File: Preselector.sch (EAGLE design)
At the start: 275 parts, among them IC4 TPS7A8101DRB, IC58 LMZ31707RVQ, Q2 FDV303N, X1 0733660061, X10 0733660061, X11 0733660061, X12 0733660061, X13 0733660061, X14 0733660061, X15 0733660061, X16 0733660061, X17 0733660061, X18 0733660061, X19 0733660061, X2 0733660061, X20 0733660061, X21 0733660061, X22 0733660061, X23 0733660061, X24 0733660061, X25 0733660061, X26 0733660061, X27 0733660061, X28 0733660061, X29 0733660061, X3 0733660061, X30 0733660061, X31 0733660061, X32 0733660061, X4 0733660061, X5 0733660061, X6 0733660061, X7 0733660061, X8 0733660061, X9 0733660061

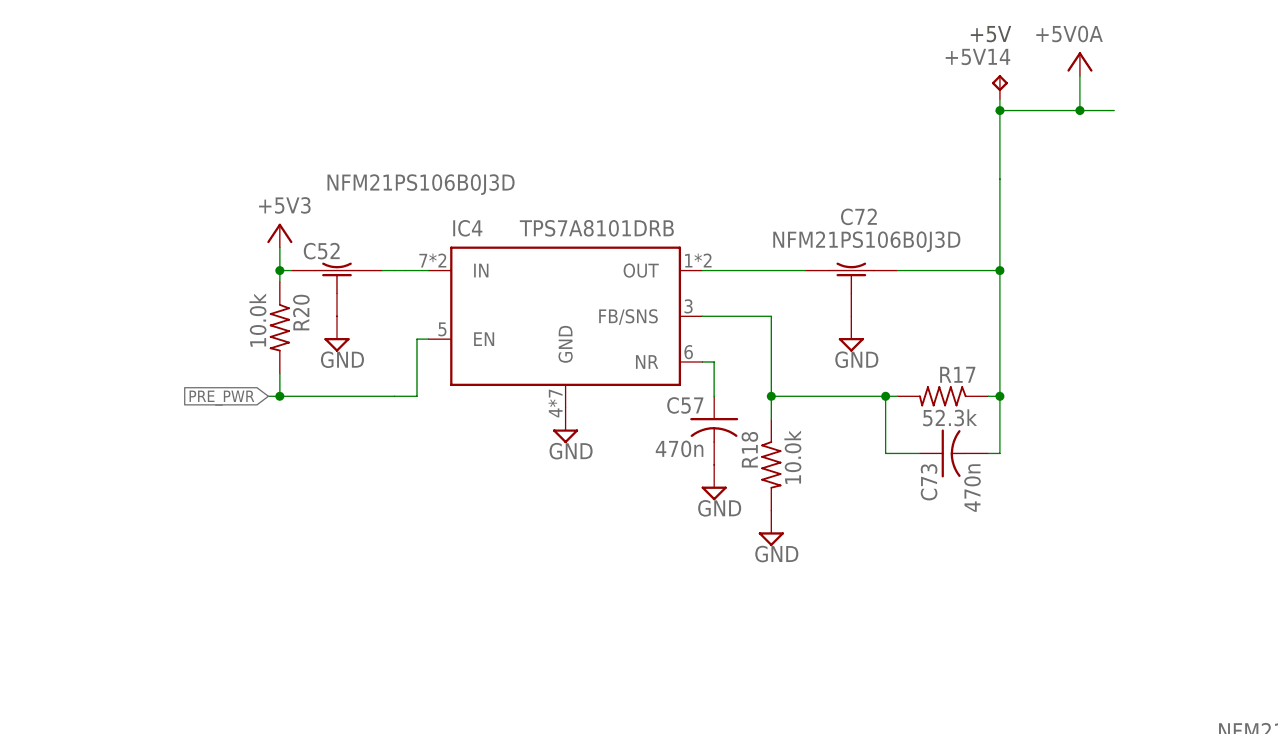
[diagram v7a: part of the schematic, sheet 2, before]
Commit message: Started laying out voltage regulator.
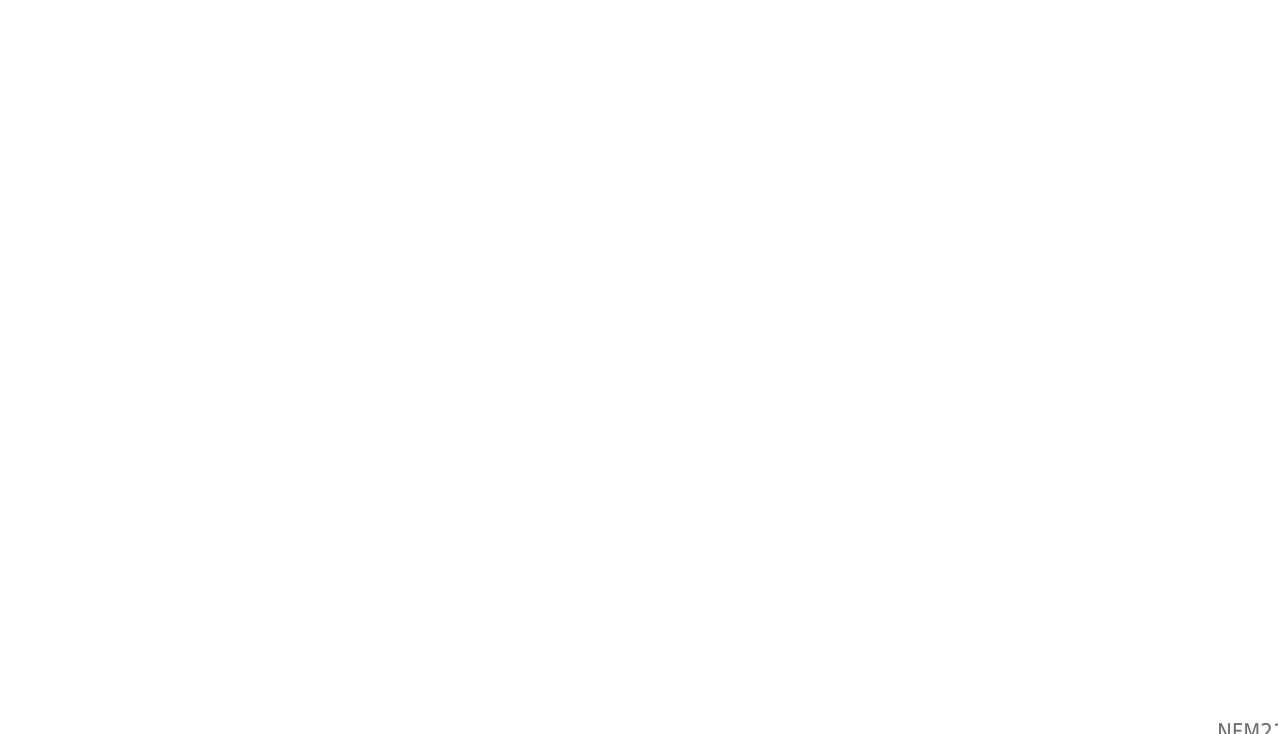
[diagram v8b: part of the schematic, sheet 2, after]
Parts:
- removed +5V14: TPTP20SQ, testpad:TPTP20SQ
- removed C52, C72: NFM21PS106B0J3D, DEEP EDDY:NFM21PS
- removed C57, C73: 470n, rcl:C-USC0402K
- removed IC4: TPS7A8101DRB, DEEP EDDY:TPS7A8101DRB
- removed R17: 52.3k, rcl:R-US_R0603
- removed R18, R20: 10.0k, rcl:R-US_R0603
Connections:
- removed net +5V0A: +5V14.TP, C72.OUT, C73.2, R17.1
- removed net N$2: C73.1, IC4.FB/SNS, R17.2, R18.1
- removed net N$3: C57.1, IC4.NR
- removed net N$4: C52.OUT, IC4.IN
- removed net N$6: C72.IN, IC4.OUT
- net +5V3: no longer C52.IN, R20.1
- net GND: no longer C52.GND, C57.2, C72.GND, IC4.GND, R18.2
- net PRE_PWR: no longer IC4.EN, R20.2
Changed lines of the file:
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@@
 <part name="SUPPLY48" library="supply2" deviceset="GND" device=""/>
 <part name="V23" library="supply2" deviceset="GND" device=""/>
-<part name="R20" library="rcl" deviceset="R-US_" device="R0603" value="10.0k"/>
-<part name="IC4" library="DEEP EDDY" deviceset="TPS7A8101" device="DRB"/>
-<part name="+5V11" library="NewSDRS" deviceset="+5V3" device=""/>
-<part name="V41" library="supply2" deviceset="GND" device=""/>
-<part name="R17" library="rcl" deviceset="R-US_" device="R0603" value="52.3k"/>
-<part name="R18" library="rcl" deviceset="R-US_" device="R0603" value="10.0k"/>
-<part name="V44" library="supply2" deviceset="GND" device=""/>
-<part name="V48" library="supply2" deviceset="GND" device=""/>
-<part name="C57" library="rcl" deviceset="C-US" device="C0402K" value="470n"/>
-<part name="C73" library="rcl" deviceset="C-US" device="C0402K" value="470n"/>
-<part name="+5V14" library="testpad" deviceset="TP" device="TP20SQ"/>
-<part name="+5V0A1" library="NewSDR" deviceset="+5V0A" device=""/>
-<part name="C52" library="DEEP EDDY" deviceset="NFM21PS" device="" value="NFM21PS106B0J3D"/>
-<part name="V24" library="supply2" deviceset="GND" device=""/>
-<part name="C72" library="DEEP EDDY" deviceset="NFM21PS" device="" value="NFM21PS106B0J3D"/>
-<part name="V25" library="supply2" deviceset="GND" device=""/>
 <part name="X26" library="con-coax" deviceset="BU-SMA-V" device="" value="0733660061"/>
 <part name="V26" library="supply2" deviceset="GND" device=""/>
@@
 <text x="214.63" y="36.83" size="1.778" layer="97">PRESEL IN
 TO FILTERS</text>
-<text x="125.73" y="354.33" size="1.778" layer="97" rot="MR0">+5V</text>
-<text x="127" y="339.09" size="1.778" layer="106">REV B HAD PCHAN FET HERE
-GROUND GATE</text>
-<text x="30.48" y="309.88" size="1.778" layer="106">ENABLE PRE_PWR FOR BITE1</text>
 <text x="139.192" y="231.14" size="1.778" layer="97" rot="MR0">+5V</text>
 <text x="226.06" y="270.51" size="1.778" layer="106">REV B HAD PCHAN FET HERE
@@
 <attribute name="VALUE" x="149.225" y="60.325" size="1.778" layer="96" rot="MR0"/>
 </instance>
-<instance part="R20" gate="G$1" x="44.45" y="322.58" rot="R270"/>
-<instance part="IC4" gate="G$1" x="76.2" y="323.85" smashed="yes">
-<attribute name="NAME" x="63.5" y="332.74" size="1.778" layer="95"/>
-<attribute name="VALUE" x="71.12" y="332.74" size="1.778" layer="96"/>
-</instance>
-<instance part="+5V11" gate="G$1" x="44.45" y="334.01" smashed="yes">
-<attribute name="VALUE" x="41.91" y="335.28" size="1.778" layer="96"/>
-</instance>
-<instance part="V41" gate="GND" x="76.2" y="311.15"/>
-<instance part="R17" gate="G$1" x="118.11" y="314.96" rot="MR0"/>
-<instance part="R18" gate="G$1" x="99.06" y="307.34" rot="MR270"/>
-<instance part="V44" gate="GND" x="99.06" y="299.72"/>
-<instance part="V48" gate="GND" x="92.71" y="304.8"/>
-<instance part="C57" gate="G$1" x="92.71" y="312.42" rot="MR0"/>
-<instance part="C73" gate="G$1" x="118.11" y="308.61" rot="MR270"/>
-<instance part="+5V14" gate="G$1" x="124.46" y="350.52" rot="MR0"/>
-<instance part="+5V0A1" gate="G$1" x="133.35" y="353.06"/>
-<instance part="C52" gate="G$1" x="50.8" y="328.93" smashed="yes">
-<attribute name="NAME" x="46.99" y="330.2" size="1.778" layer="95"/>
-<attribute name="VALUE" x="49.53" y="337.82" size="1.778" layer="96"/>
-</instance>
-<instance part="V24" gate="GND" x="50.8" y="321.31"/>
-<instance part="C72" gate="G$1" x="107.95" y="328.93" smashed="yes">
-<attribute name="NAME" x="106.68" y="334.01" size="1.778" layer="95"/>
-<attribute name="VALUE" x="99.06" y="331.47" size="1.778" layer="96"/>
-</instance>
-<instance part="V25" gate="GND" x="107.95" y="321.31"/>
 <instance part="X26" gate="G$1" x="120.65" y="177.8" smashed="yes" rot="R90">
 <attribute name="NAME" x="117.348" y="175.26" size="1.778" layer="95" rot="R90"/>
@@
 </segment>
 <segment>
-<pinref part="IC4" gate="G$1" pin="GND"/>
-<pinref part="V41" gate="GND" pin="GND"/>
-</segment>
-<segment>
-<pinref part="R18" gate="G$1" pin="2"/>
-<pinref part="V44" gate="GND" pin="GND"/>
-</segment>
-<segment>
-<pinref part="V48" gate="GND" pin="GND"/>
-<pinref part="C57" gate="G$1" pin="2"/>
-</segment>
-<segment>
-<pinref part="C52" gate="G$1" pin="GND"/>
-<pinref part="V24" gate="GND" pin="GND"/>
-</segment>
-<segment>
-<pinref part="C72" gate="G$1" pin="GND"/>
-<pinref part="V25" gate="GND" pin="GND"/>
-</segment>
-<segment>
 <pinref part="X26" gate="G$1" pin="GND"/>
 <pinref part="V26" gate="GND" pin="GND"/>
@@
 <net name="PRE_PWR" class="0">
 <segment>
-<pinref part="IC4" gate="G$1" pin="EN"/>
-<wire x1="60.96" y1="321.31" x2="59.69" y2="321.31" width="0.1524" layer="91"/>
-<wire x1="59.69" y1="321.31" x2="59.69" y2="314.96" width="0.1524" layer="91"/>
-<wire x1="59.69" y1="314.96" x2="57.15" y2="314.96" width="0.1524" layer="91"/>
-<label x="43.18" y="314.96" size="1.27" layer="91" rot="R180" xref="yes"/>
-<wire x1="57.15" y1="314.96" x2="44.45" y2="314.96" width="0.1524" layer="91"/>
-<pinref part="R20" gate="G$1" pin="2"/>
-<wire x1="44.45" y1="314.96" x2="43.18" y2="314.96" width="0.1524" layer="91"/>
-<wire x1="44.45" y1="317.5" x2="44.45" y2="314.96" width="0.1524" layer="91"/>
-<junction x="44.45" y="314.96"/>
-</segment>
-<segment>
 <pinref part="LDO_10" gate="G$1" pin="EN"/>
 <wire x1="160.02" y1="260.35" x2="158.75" y2="260.35" width="0.1524" layer="91"/>
@@
 </segment>
 </net>
-<net name="N$2" class="0">
-<segment>
-<pinref part="R17" gate="G$1" pin="2"/>
-<pinref part="IC4" gate="G$1" pin="FB/SNS"/>
-<wire x1="113.03" y1="314.96" x2="111.76" y2="314.96" width="0.1524" layer="91"/>
-<pinref part="R18" gate="G$1" pin="1"/>
-<wire x1="111.76" y1="314.96" x2="99.06" y2="314.96" width="0.1524" layer="91"/>
-<wire x1="99.06" y1="314.96" x2="99.06" y2="323.85" width="0.1524" layer="91"/>
-<wire x1="99.06" y1="323.85" x2="91.44" y2="323.85" width="0.1524" layer="91"/>
-<wire x1="99.06" y1="312.42" x2="99.06" y2="314.96" width="0.1524" layer="91"/>
-<junction x="99.06" y="314.96"/>
-<pinref part="C73" gate="G$1" pin="1"/>
-<wire x1="115.57" y1="308.61" x2="111.76" y2="308.61" width="0.1524" layer="91"/>
-<wire x1="111.76" y1="308.61" x2="111.76" y2="314.96" width="0.1524" layer="91"/>
-<junction x="111.76" y="314.96"/>
-</segment>
-</net>
-<net name="N$3" class="0">
-<segment>
-<pinref part="IC4" gate="G$1" pin="NR"/>
-<pinref part="C57" gate="G$1" pin="1"/>
-<wire x1="91.44" y1="318.77" x2="92.71" y2="318.77" width="0.1524" layer="91"/>
-<wire x1="92.71" y1="318.77" x2="92.71" y2="314.96" width="0.1524" layer="91"/>
-</segment>
-</net>
-<net name="+5V0A" class="0">
-<segment>
-<junction x="124.46" y="346.71"/>
-<wire x1="133.35" y1="346.71" x2="124.46" y2="346.71" width="0.1524" layer="91"/>
-<wire x1="124.46" y1="339.09" x2="124.46" y2="346.71" width="0.1524" layer="91"/>
-<wire x1="124.46" y1="328.93" x2="124.46" y2="339.09" width="0.1524" layer="91"/>
-<pinref part="R17" gate="G$1" pin="1"/>
-<wire x1="123.19" y1="314.96" x2="124.46" y2="314.96" width="0.1524" layer="91"/>
-<wire x1="124.46" y1="314.96" x2="124.46" y2="328.93" width="0.1524" layer="91"/>
-<pinref part="C73" gate="G$1" pin="2"/>
-<wire x1="123.19" y1="308.61" x2="124.46" y2="308.61" width="0.1524" layer="91"/>
-<wire x1="124.46" y1="308.61" x2="124.46" y2="314.96" width="0.1524" layer="91"/>
-<junction x="124.46" y="314.96"/>
-<pinref part="+5V14" gate="G$1" pin="TP"/>
-<wire x1="124.46" y1="347.98" x2="124.46" y2="346.71" width="0.1524" layer="91"/>
-<pinref part="+5V0A1" gate="G$1" pin="+5V0A"/>
-<wire x1="133.35" y1="350.52" x2="133.35" y2="346.71" width="0.1524" layer="91"/>
-<junction x="133.35" y="346.71"/>
-<pinref part="C72" gate="G$1" pin="OUT"/>
-<wire x1="113.03" y1="328.93" x2="124.46" y2="328.93" width="0.1524" layer="91"/>
-<junction x="124.46" y="328.93"/>
-<wire x1="133.35" y1="346.71" x2="137.16" y2="346.71" width="0.1524" layer="91"/>
-</segment>
-</net>
-<net name="N$4" class="0">
-<segment>
-<pinref part="IC4" gate="G$1" pin="IN"/>
-<wire x1="60.96" y1="328.93" x2="58.42" y2="328.93" width="0.1524" layer="91"/>
-<pinref part="C52" gate="G$1" pin="OUT"/>
-<wire x1="58.42" y1="328.93" x2="57.15" y2="328.93" width="0.1524" layer="91"/>
-<wire x1="57.15" y1="328.93" x2="55.88" y2="328.93" width="0.1524" layer="91"/>
-</segment>
-</net>
-<net name="N$6" class="0">
-<segment>
-<pinref part="C72" gate="G$1" pin="IN"/>
-<pinref part="IC4" gate="G$1" pin="OUT"/>
-<wire x1="102.87" y1="328.93" x2="91.44" y2="328.93" width="0.1524" layer="91"/>
-</segment>
-</net>
 <net name="SAW_14_OUT" class="0">
 <segment>
@@
 <net name="+5V3" class="0">
 <segment>
-<pinref part="C52" gate="G$1" pin="IN"/>
-<pinref part="+5V11" gate="G$1" pin="+5V3"/>
-<wire x1="45.72" y1="328.93" x2="44.45" y2="328.93" width="0.1524" layer="91"/>
-<wire x1="44.45" y1="328.93" x2="44.45" y2="331.47" width="0.1524" layer="91"/>
-<pinref part="R20" gate="G$1" pin="1"/>
-<wire x1="44.45" y1="327.66" x2="44.45" y2="328.93" width="0.1524" layer="91"/>
-<junction x="44.45" y="328.93"/>
-</segment>
-<segment>
 <pinref part="C94" gate="G$1" pin="IN"/>
